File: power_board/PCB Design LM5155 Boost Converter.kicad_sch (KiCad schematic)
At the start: 41 parts, among them Q1 BSC035N04LS G, U1 LM5155_DSSR

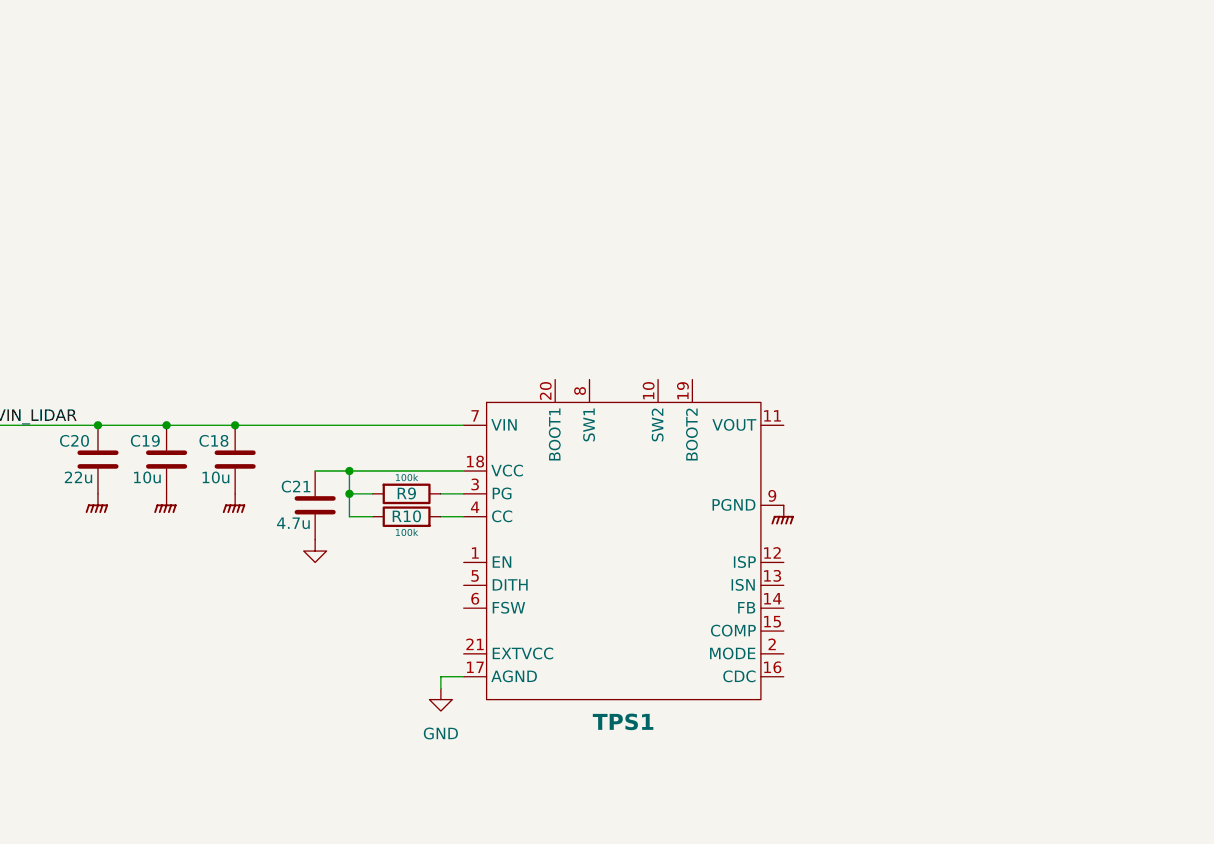
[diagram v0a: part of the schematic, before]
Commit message: Updated the LIDAR Power Supply
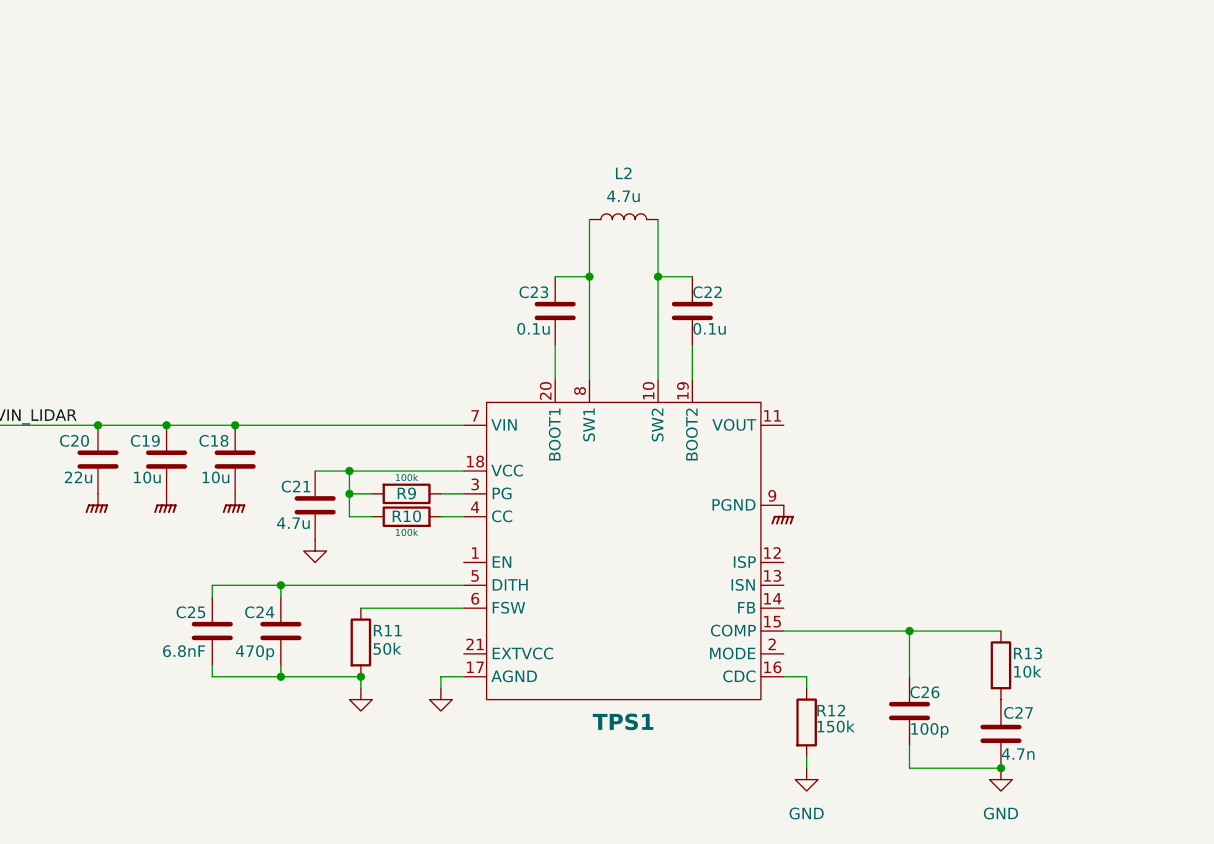
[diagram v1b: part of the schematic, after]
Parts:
- added C22, C23: 0.1u, symbol Device:C
- added C24: 470p, symbol Device:C
- added C25: 6.8nF, symbol Device:C
- added C26: 100p, symbol Device:C
- added C27: 4.7n, symbol Device:C
- added L2: 4.7u, symbol Device:L
- added R11: 50k, symbol Device:R
- added R12: 150k, symbol Device:R
- added R13: 10k, symbol Device:R
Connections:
- net GND: now also C24.2, C25.2, C26.2, C27.2, R11.2, R12.2
- net at TPS1.10 (SW2): now also C22.1, L2.2
- net at TPS1.15 (COMP): now also C26.1, R13.1
- net at TPS1.16 (CDC): now also R12.1
- net at TPS1.19 (BOOT2): now also C22.2
- net at TPS1.20 (BOOT1): now also C23.2
- net at TPS1.5 (DITH): now also C24.1, C25.1
- net at TPS1.6 (FSW): now also R11.1
- net at TPS1.8 (SW1): now also C23.1, L2.1
- new net: C27.1, R13.2

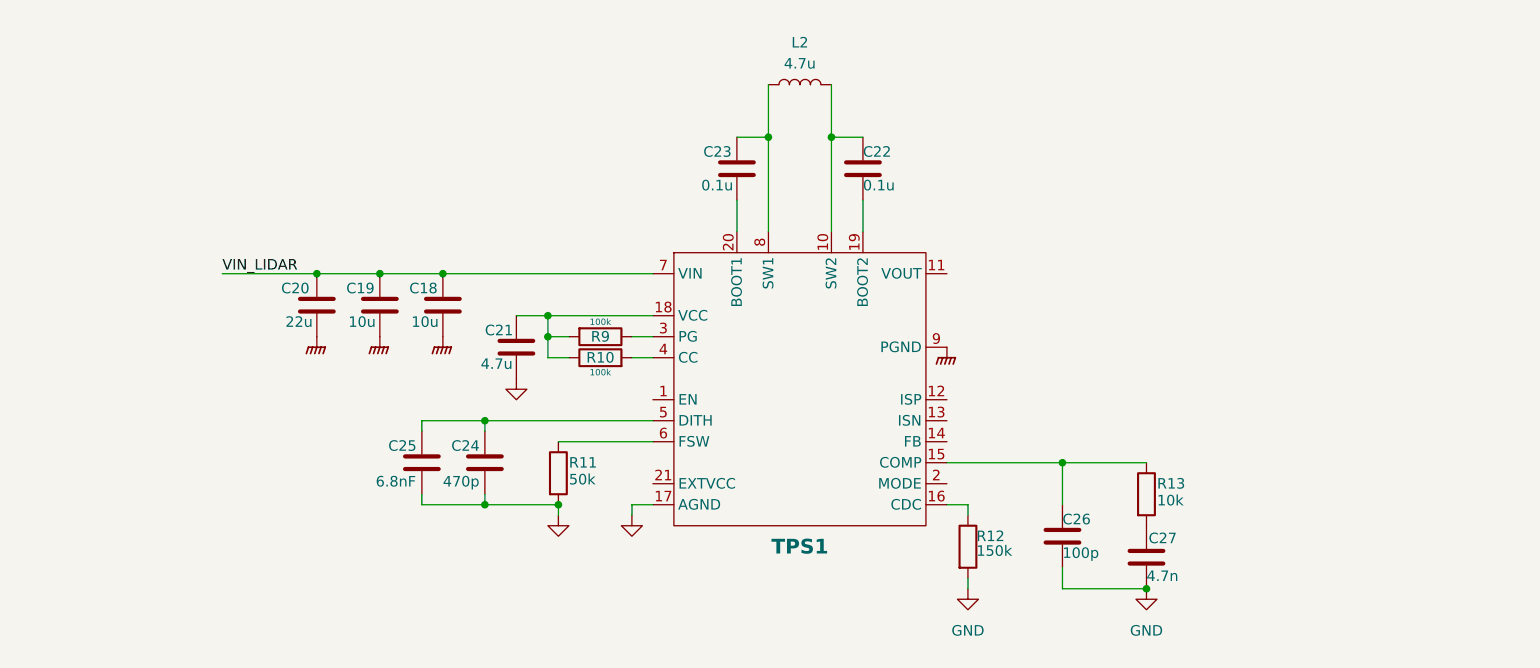
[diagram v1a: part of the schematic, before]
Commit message: Completed Schematic for LIDAR Power
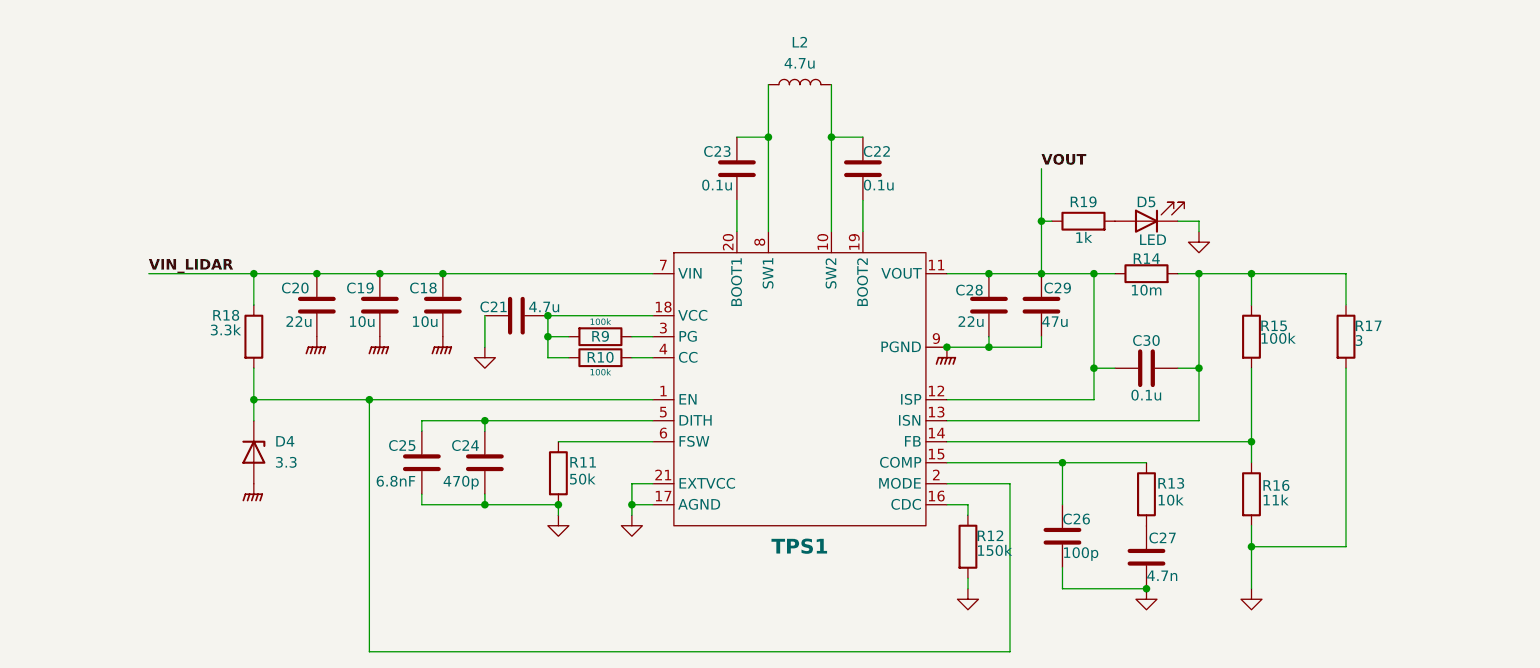
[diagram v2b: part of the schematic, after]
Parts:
- added C28: 22u, symbol Device:C
- added C29: 47u, symbol Device:C
- added C30: 0.1u, symbol Device:C
- added D4: 3.3, symbol Device:D_Zener
- added D5: LED, symbol Device:LED
- added R14: 10m, symbol Device:R
- added R15: 100k, symbol Device:R
- added R16: 11k, symbol Device:R
- added R17: 3, symbol Device:R
- added R18: 3.3k, symbol Device:R
- added R19: 1k, symbol Device:R
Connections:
- net GND: now also C21.1, TPS1.21 (EXTVCC), C28.2, C29.2, D4.2 (A), D5.1 (K), R16.2, R17.2; no longer C21.2
- net VIN_LIDAR: now also R18.1
- net at R10.1, R9.2, TPS1.18 (VCC): now also C21.2; no longer C21.1
- net at TPS1.1 (EN): now also TPS1.2 (MODE), D4.1 (K), R18.2
- net VOUT: now reaches TPS1.11 (VOUT)
- net VOUT: now also TPS1.12 (ISP), C28.1, C29.1, C30.1, R14.1, R19.1
- net at TPS1.13 (ISN): now also C30.2, R14.2, R15.1, R17.1
- net at TPS1.14 (FB): now also R15.2, R16.1
- new net: D5.2 (A), R19.2
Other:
- moved on the sheet: C21

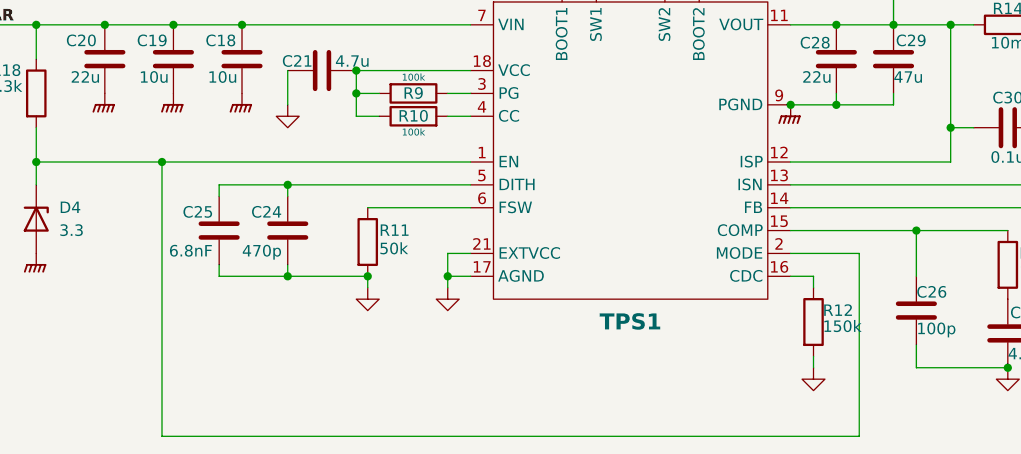
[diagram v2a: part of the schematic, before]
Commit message: Updated PCB Schematic
Moved the LM5155 to the right
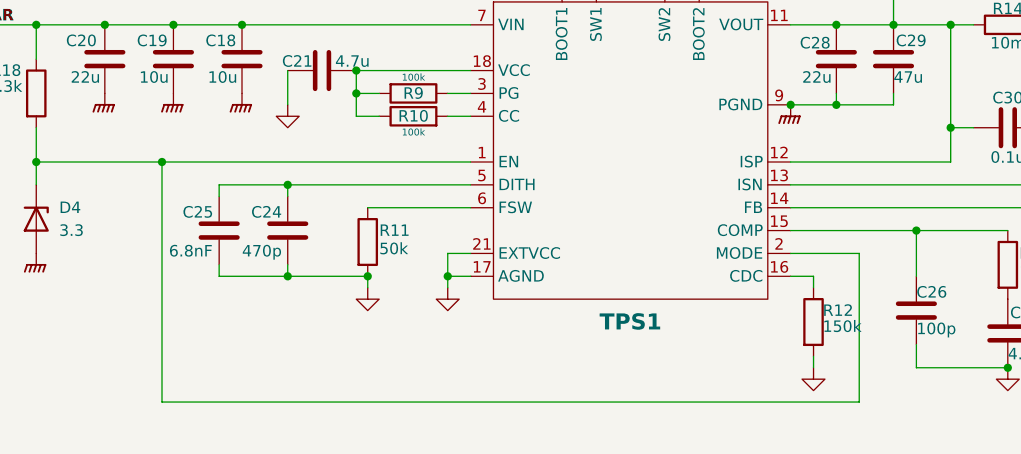
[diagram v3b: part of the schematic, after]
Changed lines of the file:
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@@
+	)
+	(junction
+		(at 300.99 90.805)
+		(diameter 0)
+		(color 0 0 0 0)
+	)
+	(junction
+		(at 152.4 154.305)
+		(diameter 0)
+		(color 0 0 0 0)
+	)
+	(junction
+		(at 189.23 256.54)
+		(diameter 0)
+		(color 0 0 0 0)
+	)
+	(junction
+		(at 336.55 62.865)
+		(diameter 0)
+		(color 0 0 0 0)
+	)
+	(junction
+		(at 130.81 219.71)
+		(diameter 0)
+		(color 0 0 0 0)
+	)
+	(junction
+		(at 96.52 264.16)
+		(diameter 0)
+		(color 0 0 0 0)
+	)
+	(junction
+		(at 353.06 62.865)
+		(diameter 0)
+		(color 0 0 0 0)
+	)
+	(junction
+		(at 300.99 68.58)
+		(diameter 0)
+		(color 0 0 0 0)
+	)
+	(junction
+		(at 367.03 62.865)
+		(diameter 0)
+		(color 0 0 0 0)
+	)
+	(junction
+		(at 119.38 109.855)
+		(diameter 0)
+		(color 0 0 0 0)
+	)
+	(junction
+		(at 104.14 243.84)
+		(diameter 0)
+		(color 0 0 0 0)
+	)
+	(junction
+		(at 91.44 236.22)
+		(diameter 0)
+		(color 0 0 0 0)
+	)
+	(junction
+		(at 222.25 49.53)
+		(diameter 0)
+		(color 0 0 0 0)
+	)
+	(junction
+		(at 346.71 49.53)
+		(diameter 0)
+		(color 0 0 0 0)
+	)
+	(junction
+		(at 166.37 259.08)
+		(diameter 0)
+		(color 0 0 0 0)
+	)
+	(junction
+		(at 170.18 236.22)
+		(diameter 0)
+		(color 0 0 0 0)
+	)
+	(junction
+		(at 76.2 236.22)
+		(diameter 0)
+		(color 0 0 0 0)
+	)
+	(junction
+		(at 356.87 49.53)
+		(diameter 0)
+		(color 0 0 0 0)
+	)
+	(junction
+		(at 157.48 236.22)
+		(diameter 0)
+		(color 0 0 0 0)
+	)
+	(junction
+		(at 219.71 127.635)
+		(diameter 0)
+		(color 0 0 0 0)
+	)
+	(junction
+		(at 105.41 264.16)
+		(diameter 0)
+		(color 0 0 0 0)
+	)
+	(junction
+		(at 228.6 141.605)
+		(diameter 0)
+		(color 0 0 0 0)
+	)
+	(junction
+		(at 104.14 241.3)
+		(diameter 0)
+		(color 0 0 0 0)
+	)
+	(junction
+		(at 96.52 254)
+		(diameter 0)
+		(color 0 0 0 0)
+	)
+	(junction
+		(at 114.3 264.16)
+		(diameter 0)
+		(color 0 0 0 0)
+	)
+	(junction
+		(at 68.58 236.22)
+		(diameter 0)
+		(color 0 0 0 0)
+	)
+	(junction
+		(at 356.87 62.865)
+		(diameter 0)
+		(color 0 0 0 0)
+	)
+	(junction
+		(at 157.48 245.11)
+		(diameter 0)
+		(color 0 0 0 0)
+	)
+	(junction
+		(at 83.82 236.22)
+		(diameter 0)
+		(color 0 0 0 0)
+	)
+	(junction
+		(at 68.58 251.46)
+		(diameter 0)
+		(color 0 0 0 0)
+	)
+	(junction
+		(at 391.16 49.53)
+		(diameter 0)
+		(color 0 0 0 0)
+	)
+	(junction
+		(at 228.6 127.635)
+		(diameter 0)
+		(color 0 0 0 0)
+	)
+	(junction
+		(at 182.88 247.65)
+		(diameter 0)
+		(color 0 0 0 0)
+	)
+	(junction
+		(at 403.86 62.865)
+		(diameter 0)
+		(color 0 0 0 0)
+	)
+	(junction
+		(at 155.575 106.68)
+		(diameter 0)
+		(color 0 0 0 0)
+	)
+	(junction
+		(at 367.03 49.53)
+		(diameter 0)
+		(color 0 0 0 0)
+	)
+	(junction
+		(at 52.705 96.52)
+		(diameter 0)
+		(color 0 0 0 0)
+	)
+	(junction
+		(at 163.83 229.87)
+		(diameter 0)
+		(color 0 0 0 0)
+	)
+	(junction
+		(at 377.19 49.53)
+		(diameter 0)
+		(color 0 0 0 0)
+	)
+	(junction
+		(at 152.4 127.635)
+		(diameter 0)
+		(color 0 0 0 0)
+	)
+	(junction
+		(at 138.43 219.71)
+		(diameter 0)
+		(color 0 0 0 0)
 	)
 	(junction
 		(at 82.55 251.46)
-		(diameter 0)
-		(color 0 0 0 0)
-	)
-	(junction
-		(at 300.99 90.805)
-		(diameter 0)
-		(color 0 0 0 0)
-	)
-	(junction
-		(at 152.4 154.305)
-		(diameter 0)
-		(color 0 0 0 0)
-	)
-	(junction
-		(at 189.23 256.54)
-		(diameter 0)
-		(color 0 0 0 0)
-	)
-	(junction
-		(at 336.55 62.865)
-		(diameter 0)
-		(color 0 0 0 0)
-	)
-	(junction
-		(at 130.81 219.71)
-		(diameter 0)
-		(color 0 0 0 0)
-	)
-	(junction
-		(at 96.52 264.16)
-		(diameter 0)
-		(color 0 0 0 0)
-	)
-	(junction
-		(at 353.06 62.865)
-		(diameter 0)
-		(color 0 0 0 0)
-	)
-	(junction
-		(at 300.99 68.58)
-		(diameter 0)
-		(color 0 0 0 0)
-	)
-	(junction
-		(at 367.03 62.865)
-		(diameter 0)
-		(color 0 0 0 0)
-	)
-	(junction
-		(at 119.38 109.855)
-		(diameter 0)
-		(color 0 0 0 0)
-	)
-	(junction
-		(at 104.14 243.84)
-		(diameter 0)
-		(color 0 0 0 0)
-	)
-	(junction
-		(at 91.44 236.22)
-		(diameter 0)
-		(color 0 0 0 0)
-	)
-	(junction
-		(at 222.25 49.53)
-		(diameter 0)
-		(color 0 0 0 0)
-	)
-	(junction
-		(at 346.71 49.53)
-		(diameter 0)
-		(color 0 0 0 0)
-	)
-	(junction
-		(at 166.37 259.08)
-		(diameter 0)
-		(color 0 0 0 0)
-	)
-	(junction
-		(at 170.18 236.22)
-		(diameter 0)
-		(color 0 0 0 0)
-	)
-	(junction
-		(at 76.2 236.22)
-		(diameter 0)
-		(color 0 0 0 0)
-	)
-	(junction
-		(at 356.87 49.53)
-		(diameter 0)
-		(color 0 0 0 0)
-	)
-	(junction
-		(at 157.48 236.22)
-		(diameter 0)
-		(color 0 0 0 0)
-	)
-	(junction
-		(at 219.71 127.635)
-		(diameter 0)
-		(color 0 0 0 0)
-	)
-	(junction
-		(at 105.41 264.16)
-		(diameter 0)
-		(color 0 0 0 0)
-	)
-	(junction
-		(at 228.6 141.605)
-		(diameter 0)
-		(color 0 0 0 0)
-	)
-	(junction
-		(at 104.14 241.3)
-		(diameter 0)
-		(color 0 0 0 0)
-	)
-	(junction
-		(at 96.52 254)
-		(diameter 0)
-		(color 0 0 0 0)
-	)
-	(junction
-		(at 114.3 264.16)
-		(diameter 0)
-		(color 0 0 0 0)
-	)
-	(junction
-		(at 68.58 236.22)
-		(diameter 0)
-		(color 0 0 0 0)
-	)
-	(junction
-		(at 356.87 62.865)
-		(diameter 0)
-		(color 0 0 0 0)
-	)
-	(junction
-		(at 157.48 245.11)
-		(diameter 0)
-		(color 0 0 0 0)
-	)
-	(junction
-		(at 83.82 236.22)
-		(diameter 0)
-		(color 0 0 0 0)
-	)
-	(junction
-		(at 68.58 251.46)
-		(diameter 0)
-		(color 0 0 0 0)
-	)
-	(junction
-		(at 391.16 49.53)
-		(diameter 0)
-		(color 0 0 0 0)
-	)
-	(junction
-		(at 228.6 127.635)
-		(diameter 0)
-		(color 0 0 0 0)
-	)
-	(junction
-		(at 182.88 247.65)
-		(diameter 0)
-		(color 0 0 0 0)
-	)
-	(junction
-		(at 403.86 62.865)
-		(diameter 0)
-		(color 0 0 0 0)
-	)
-	(junction
-		(at 155.575 106.68)
-		(diameter 0)
-		(color 0 0 0 0)
-	)
-	(junction
-		(at 367.03 49.53)
-		(diameter 0)
-		(color 0 0 0 0)
-	)
-	(junction
-		(at 52.705 96.52)
-		(diameter 0)
-		(color 0 0 0 0)
-	)
-	(junction
-		(at 163.83 229.87)
-		(diameter 0)
-		(color 0 0 0 0)
-	)
-	(junction
-		(at 377.19 49.53)
-		(diameter 0)
-		(color 0 0 0 0)
-	)
-	(junction
-		(at 152.4 127.635)
-		(diameter 0)
-		(color 0 0 0 0)
-	)
-	(junction
-		(at 138.43 219.71)
 		(diameter 0)
 		(color 0 0 0 0)
@@
 	(wire
 		(pts
-			(xy 82.55 251.46) (xy 82.55 281.94)
+			(xy 82.55 251.46) (xy 82.55 278.13)
 		)
 		(stroke
@@
 	(wire
 		(pts
-			(xy 82.55 281.94) (xy 160.02 281.94)
+			(xy 82.55 278.13) (xy 160.02 278.13)
 		)
 		(stroke
@@
 	(wire
 		(pts
-			(xy 160.02 281.94) (xy 160.02 261.62)
-		)
-		(stroke
+			(xy 160.02 278.13) (xy 160.02 261.62)
+		)
+		(stroke
